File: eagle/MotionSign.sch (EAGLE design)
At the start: 77 parts, among them Q1 16MHZ, U1 ATMEGA328, U2 L7805CDT-TR, U3 NCS36000, U4 PIR, U5 WS2801, U6 SPX3819, U7 NJVMJD2955T4G, U8 TXB0108PWR, U9 LCD-HD4478020X4-4HOLES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

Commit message: Swap out power managment resistor with 204/7 for
Allow for further experimentation with power managment
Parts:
- R15: device MotionSign:R-US_M0805 -> MotionSign:R-US_0204/7
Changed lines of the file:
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@@
 <part name="SUPPLY11" library="MotionSign" library_urn="urn:adsk.eagle:library:3048452" deviceset="VCC" device=""/>
 <part name="U7" library="MotionSign" library_urn="urn:adsk.eagle:library:3048452" deviceset="NJVMJD2955T4G" device="" package3d_urn="urn:adsk.eagle:package:3048862/2"/>
-<part name="R15" library="MotionSign" library_urn="urn:adsk.eagle:library:3048452" deviceset="R-US_" device="M0805" package3d_urn="urn:adsk.eagle:package:3049036/2" value="22"/>
+<part name="R15" library="MotionSign" library_urn="urn:adsk.eagle:library:3048452" deviceset="R-US_" device="0204/7" package3d_urn="urn:adsk.eagle:package:3048939/2" value="22"/>
 <part name="GND22" library="MotionSign" library_urn="urn:adsk.eagle:library:3048452" deviceset="GND" device=""/>
 <part name="S3" library="MotionSign" library_urn="urn:adsk.eagle:library:3048452" deviceset="MOMENTARY-SWITCH-SPST" device="-SMD-5.2-REDUNDANT" package3d_urn="urn:adsk.eagle:package:3048933/2" value="Reset"/>

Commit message: Add Sensitivity/Ossilation Names
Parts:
- renumbered R7 to R7/SEN, R8 to R8/OSC
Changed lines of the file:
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@@
 <part name="C9" library="MotionSign" library_urn="urn:adsk.eagle:library:3048452" deviceset="C-US" device="C0805" package3d_urn="urn:adsk.eagle:package:3049016/2" value="10nF"/>
 <part name="GND13" library="MotionSign" library_urn="urn:adsk.eagle:library:3048452" deviceset="GND" device=""/>
-<part name="R7" library="MotionSign" library_urn="urn:adsk.eagle:library:3048452" deviceset="TRIMPOT" device="TX33X-1M" package3d_urn="urn:adsk.eagle:package:3049112/2" value="1M"/>
+<part name="R7/SEN" library="MotionSign" library_urn="urn:adsk.eagle:library:3048452" deviceset="TRIMPOT" device="TX33X-1M" package3d_urn="urn:adsk.eagle:package:3049112/2" value="1M"/>
 <part name="C11" library="MotionSign" library_urn="urn:adsk.eagle:library:3048452" deviceset="C-US" device="C0805" package3d_urn="urn:adsk.eagle:package:3049016/2" value="0.1uF"/>
 <part name="SUPPLY4" library="MotionSign" library_urn="urn:adsk.eagle:library:3048452" deviceset="VCC" device=""/>
 <part name="GND14" library="MotionSign" library_urn="urn:adsk.eagle:library:3048452" deviceset="GND" device=""/>
-<part name="R8" library="MotionSign" library_urn="urn:adsk.eagle:library:3048452" deviceset="TRIMPOT" device="TX33X-1M" package3d_urn="urn:adsk.eagle:package:3049112/2" value="1M"/>
+<part name="R8/OSC" library="MotionSign" library_urn="urn:adsk.eagle:library:3048452" deviceset="TRIMPOT" device="TX33X-1M" package3d_urn="urn:adsk.eagle:package:3049112/2" value="1M"/>
 <part name="R9" library="MotionSign" library_urn="urn:adsk.eagle:library:3048452" deviceset="R-US_" device="M0805" package3d_urn="urn:adsk.eagle:package:3049036/2" value="51k"/>
 <part name="TP1" library="MotionSign" library_urn="urn:adsk.eagle:library:3048452" deviceset="TEST-POINT" device="3X5" package3d_urn="urn:adsk.eagle:package:3048905/1" value="TEST-POINT3X5"/>
@@
 <instance part="C9" gate="G$1" x="53.34" y="68.58" rot="R90"/>
 <instance part="GND13" gate="1" x="7.62" y="30.48"/>
-<instance part="R7" gate="R?" x="53.34" y="55.88" smashed="yes" rot="MR0">
+<instance part="R7/SEN" gate="R?" x="53.34" y="55.88" smashed="yes" rot="MR0">
 <attribute name="NAME" x="53.594" y="57.15" size="1.778" layer="95"/>
 <attribute name="VALUE" x="52.578" y="57.15" size="1.778" layer="96" rot="MR0"/>
@@
 <instance part="SUPPLY4" gate="1" x="106.68" y="83.82"/>
 <instance part="GND14" gate="1" x="106.68" y="38.1"/>
-<instance part="R8" gate="R?" x="106.68" y="73.66" smashed="yes" rot="R90">
+<instance part="R8/OSC" gate="R?" x="106.68" y="73.66" smashed="yes" rot="R90">
 <attribute name="NAME" x="107.95" y="73.406" size="1.778" layer="95" rot="R270"/>
 <attribute name="VALUE" x="107.95" y="74.422" size="1.778" layer="96" rot="MR90"/>
@@
 </segment>
 <segment>
-<pinref part="R8" gate="R?" pin="WIPER"/>
+<pinref part="R8/OSC" gate="R?" pin="WIPER"/>
 <wire x1="101.6" y1="73.66" x2="99.06" y2="73.66" width="0.1524" layer="91"/>
 <wire x1="99.06" y1="73.66" x2="99.06" y2="81.28" width="0.1524" layer="91"/>
@@
 <pinref part="SUPPLY4" gate="1" pin="VCC"/>
 <wire x1="106.68" y1="81.28" x2="106.68" y2="83.82" width="0.1524" layer="91"/>
-<pinref part="R8" gate="R?" pin="CW"/>
+<pinref part="R8/OSC" gate="R?" pin="CW"/>
 <wire x1="106.68" y1="78.74" x2="106.68" y2="81.28" width="0.1524" layer="91"/>
 <junction x="106.68" y="81.28"/>
@@
 <pinref part="U3" gate="G$1" pin="OP2_N"/>
 <wire x1="45.72" y1="53.34" x2="63.5" y2="53.34" width="0.1524" layer="91"/>
-<pinref part="R7" gate="R?" pin="WIPER"/>
+<pinref part="R7/SEN" gate="R?" pin="WIPER"/>
 <wire x1="53.34" y1="60.96" x2="53.34" y2="63.5" width="0.1524" layer="91"/>
 <wire x1="53.34" y1="63.5" x2="45.72" y2="63.5" width="0.1524" layer="91"/>
@@
 <junction x="45.72" y="63.5"/>
 <junction x="45.72" y="68.58"/>
-<pinref part="R7" gate="R?" pin="CW"/>
+<pinref part="R7/SEN" gate="R?" pin="CW"/>
 <wire x1="48.26" y1="55.88" x2="45.72" y2="55.88" width="0.1524" layer="91"/>
 <junction x="45.72" y="55.88"/>
@@
 <segment>
 <pinref part="R9" gate="G$1" pin="2"/>
-<pinref part="R8" gate="R?" pin="CCW"/>
+<pinref part="R8/OSC" gate="R?" pin="CCW"/>
 <wire x1="106.68" y1="66.04" x2="106.68" y2="68.58" width="0.1524" layer="91"/>
 </segment>
@@
 <junction x="60.96" y="68.58"/>
 <label x="63.5" y="68.58" size="1.27" layer="95" xref="yes"/>
-<pinref part="R7" gate="R?" pin="CCW"/>
+<pinref part="R7/SEN" gate="R?" pin="CCW"/>
 <wire x1="58.42" y1="55.88" x2="60.96" y2="55.88" width="0.1524" layer="91"/>
 <junction x="60.96" y="55.88"/>

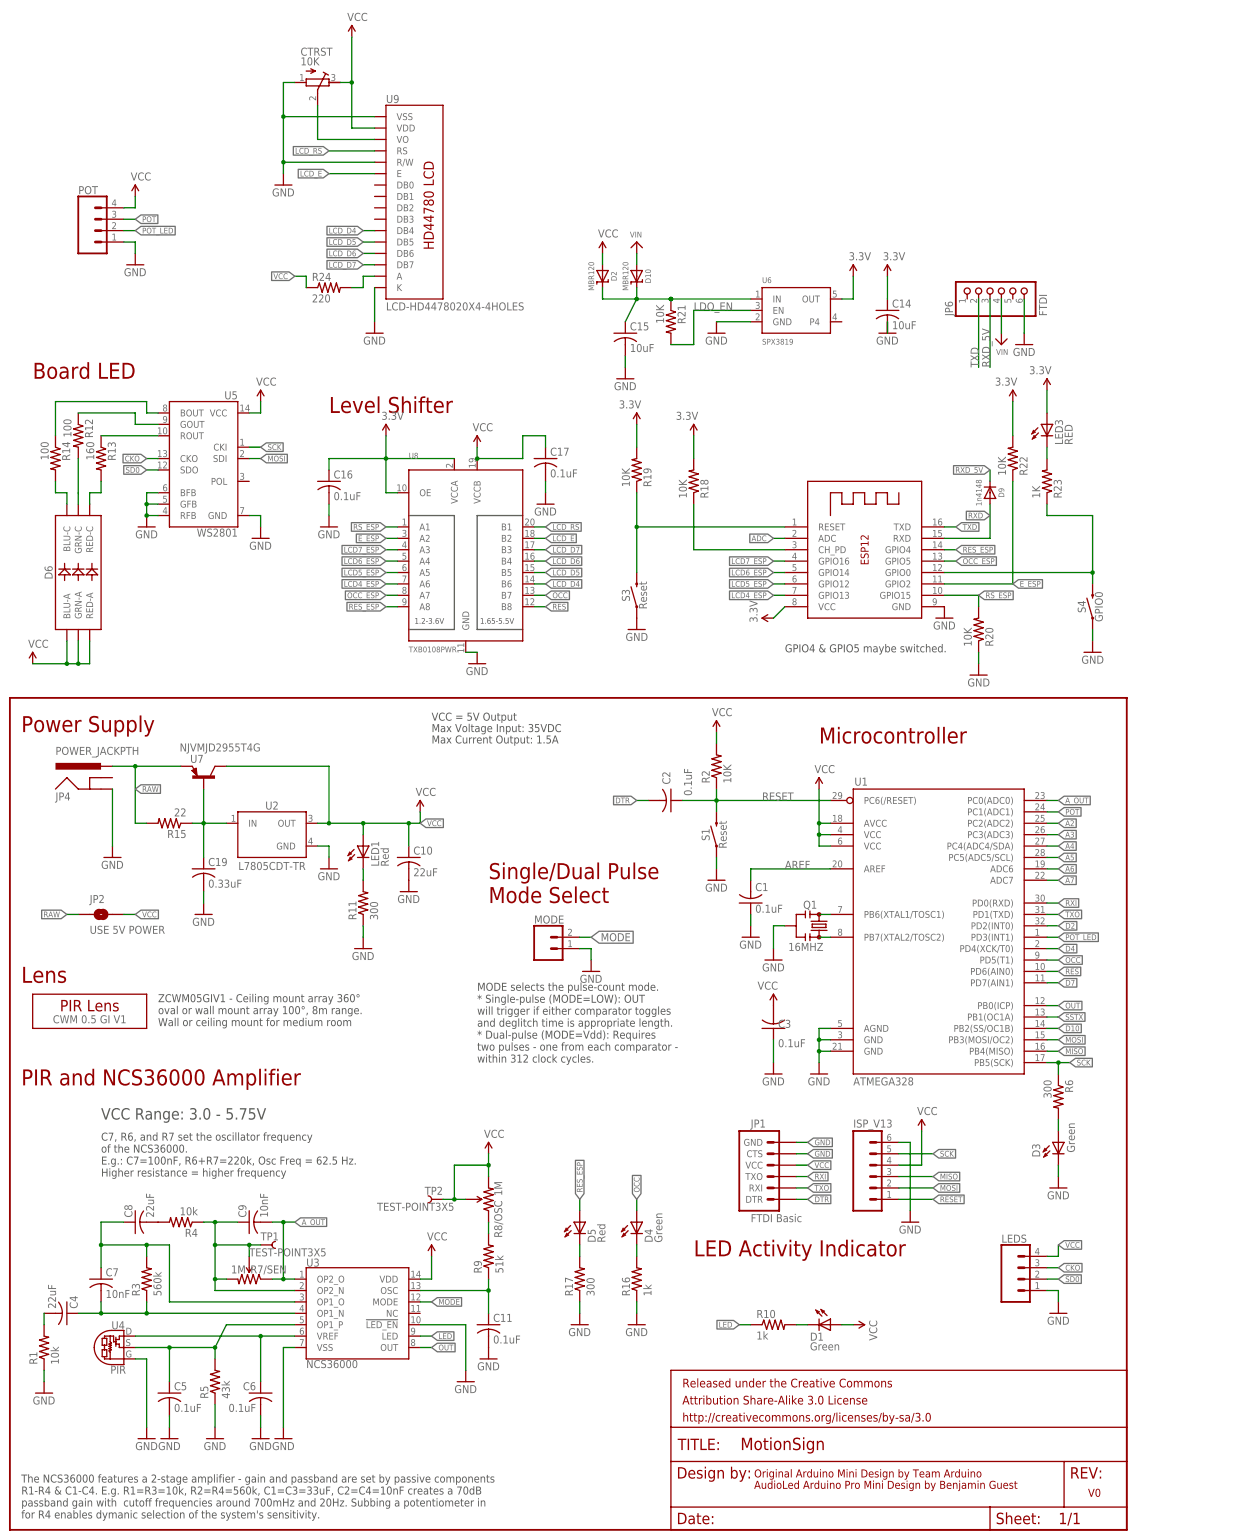
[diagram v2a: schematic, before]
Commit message: Add door reed switch
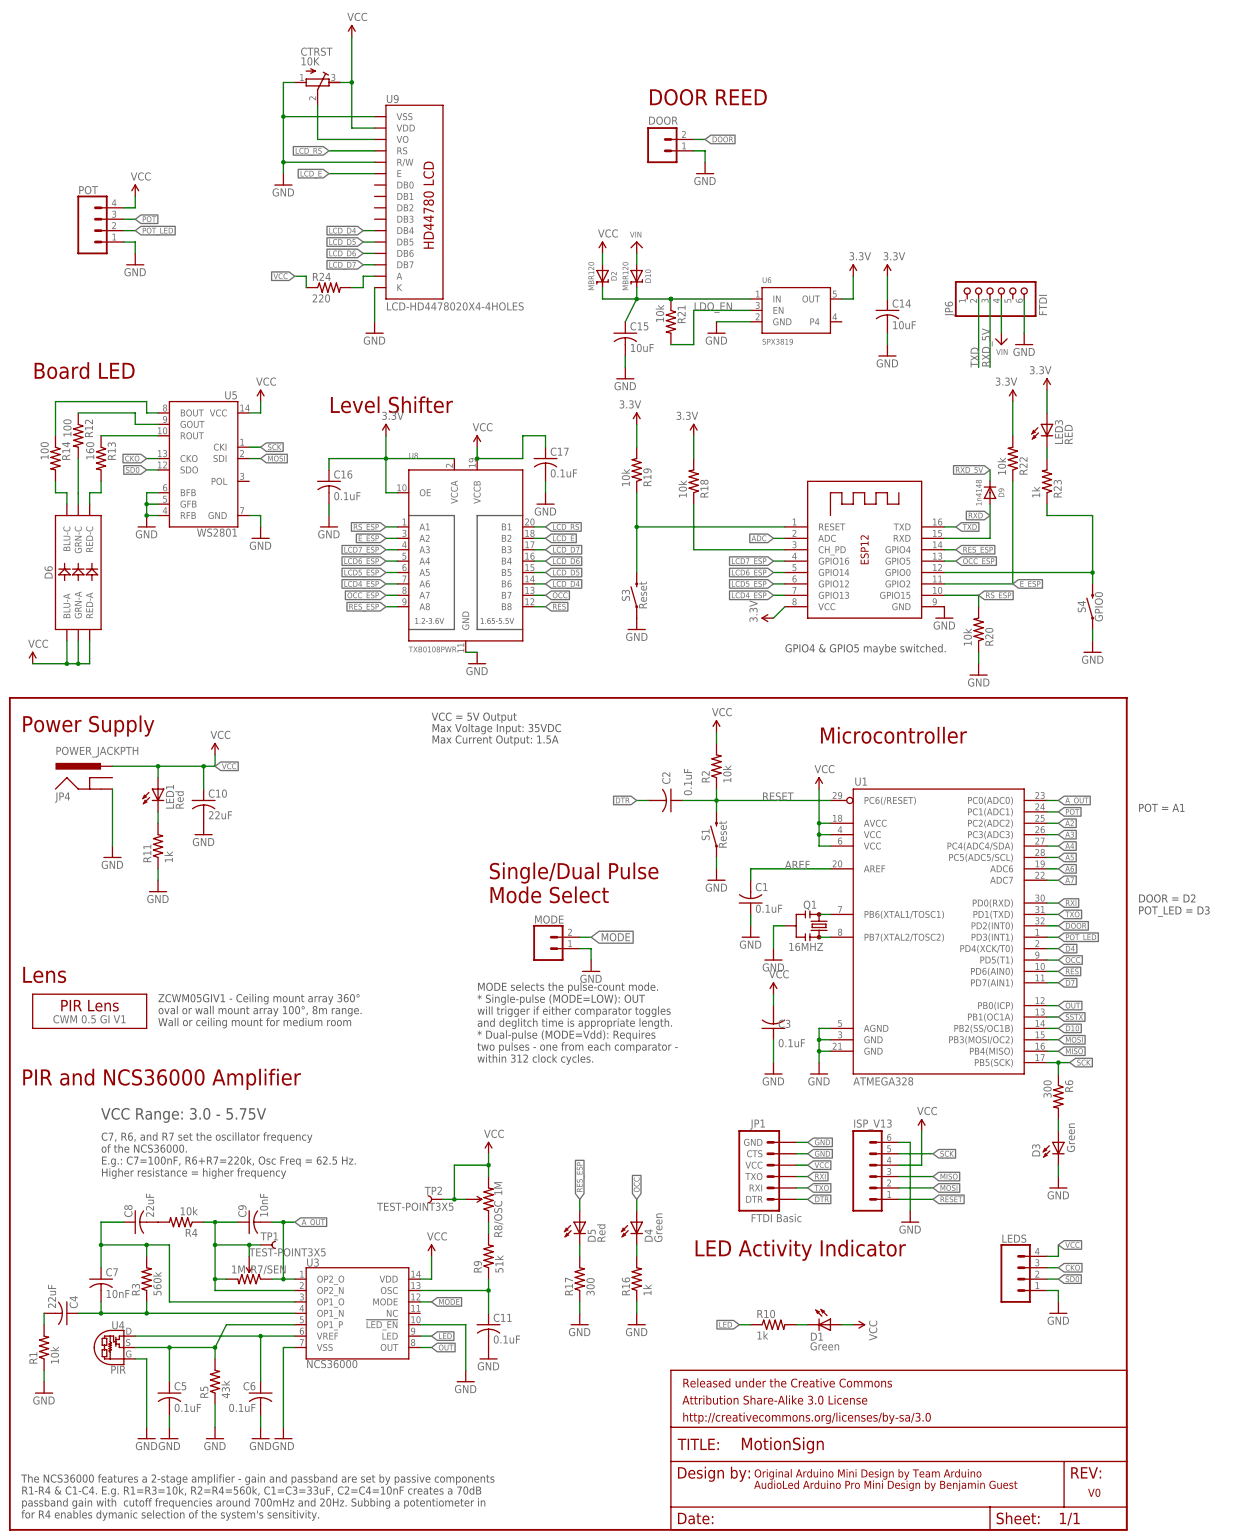
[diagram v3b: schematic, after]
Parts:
- removed C19: 0.33uF, MotionSign:C-USC0805
- removed JP2: USE 5V POWER, MotionSign:JUMPER-SMT_2_NO_SILK
- removed R15: 22, MotionSign:R-US_0204/7
- removed U2: L7805CDT-TR, MotionSign:L7805CDT-TR
- removed U7: NJVMJD2955T4G, MotionSign:NJVMJD2955T4G
- added DOOR: (no value), MotionSign:CONN_02JST-PTH-2
- R11: value 300 -> 1k
- R18, R19, R2, R20, R21, R22: value 10K -> 10k
- R23: value 1K -> 1k
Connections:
- removed net D2: U1.PD2(INT0)
- removed net L7805_IN: C19.1, R15.1, U2.IN, U7.B
- removed net RAW: JP2.1, JP4.PWR, R15.2, U7.E
- new net DOOR: DOOR.2, U1.PD2(INT0)
- net GND: now also DOOR.1; no longer C19.2, U2.GND
- net VCC: now also JP4.PWR; no longer JP2.2, U2.OUT, U7.C
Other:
- note added: "DOOR = D2 POT_LED = D3"
- note added: "DOOR REED"
- note added: "POT = A1"
- moved on the sheet: C10, LED1, R11
